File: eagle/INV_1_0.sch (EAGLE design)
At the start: 12 parts, among them IC1 74HC04N, IC2 74HC04N, X1 In A, X2 In B, X3 Out A, X4 Out B

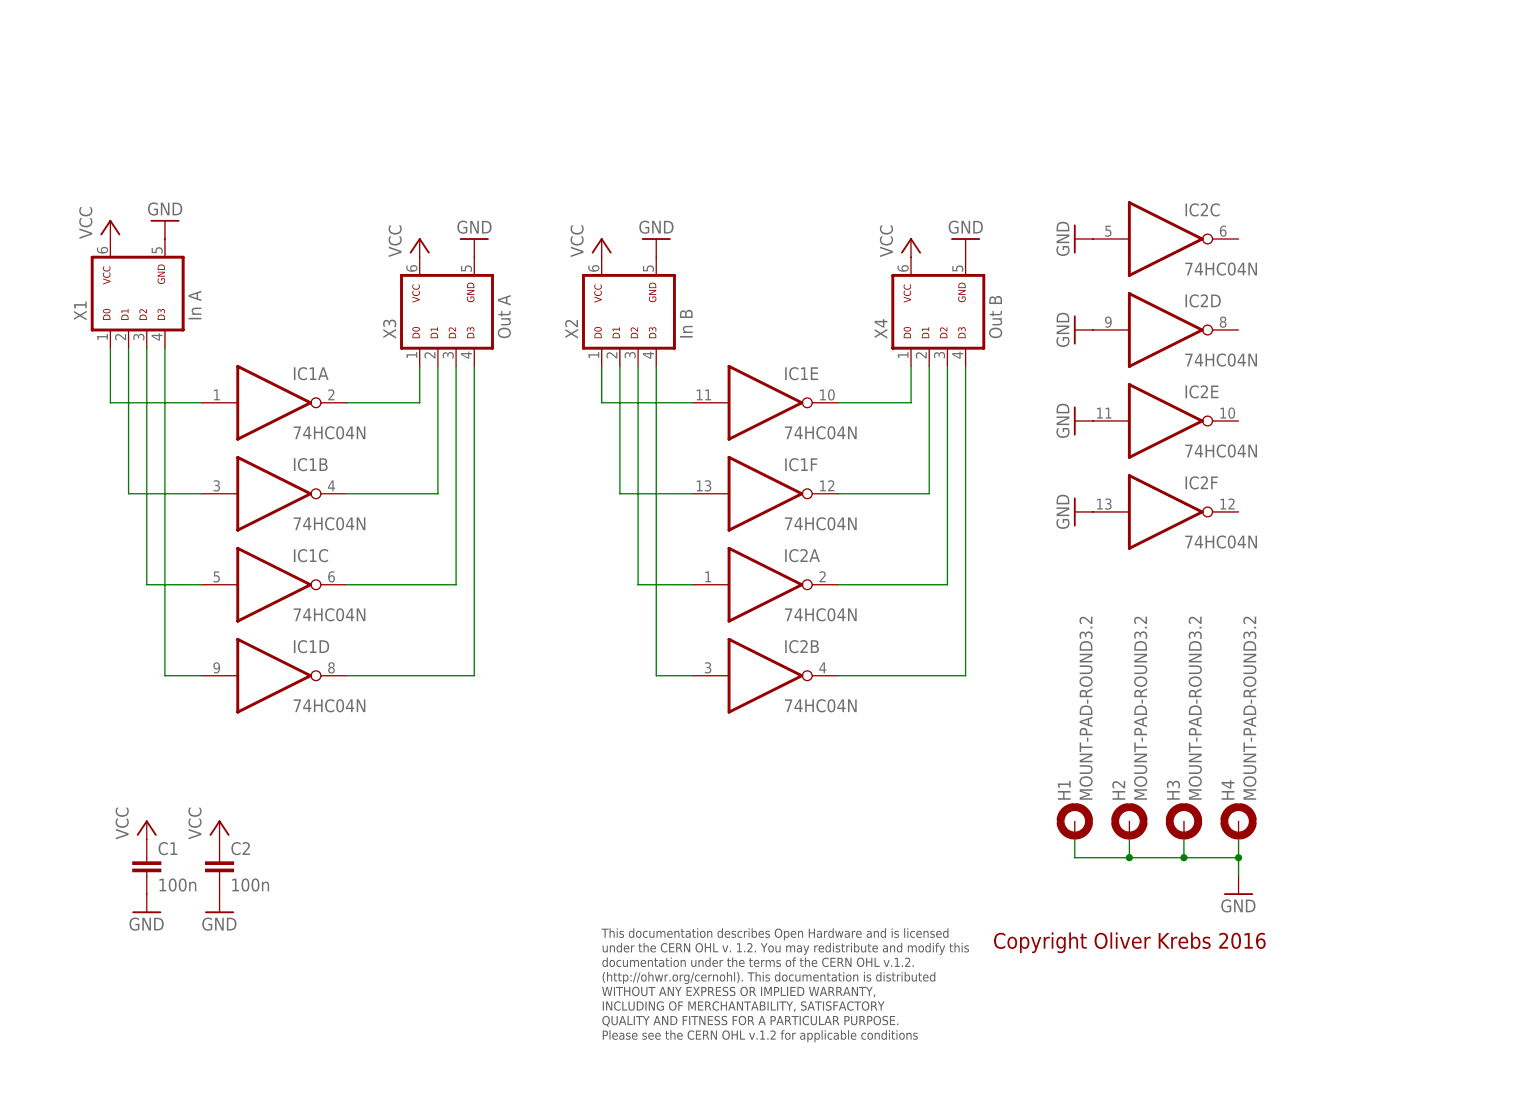
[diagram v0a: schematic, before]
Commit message: Add new tetra-Board and arduino files
Add AMP_1_0, AVC_1_0, D18_1_1, IOP_1_2, MIC_1_0, PIN_1_1, POT_1_0, PWA_1_0, PWR_1_0, RGF 2.0, SOC_2_0, VLT_1_0
Add mex_nano_shield_keyboard, mex_nano_shied_numbers

New arduino projects
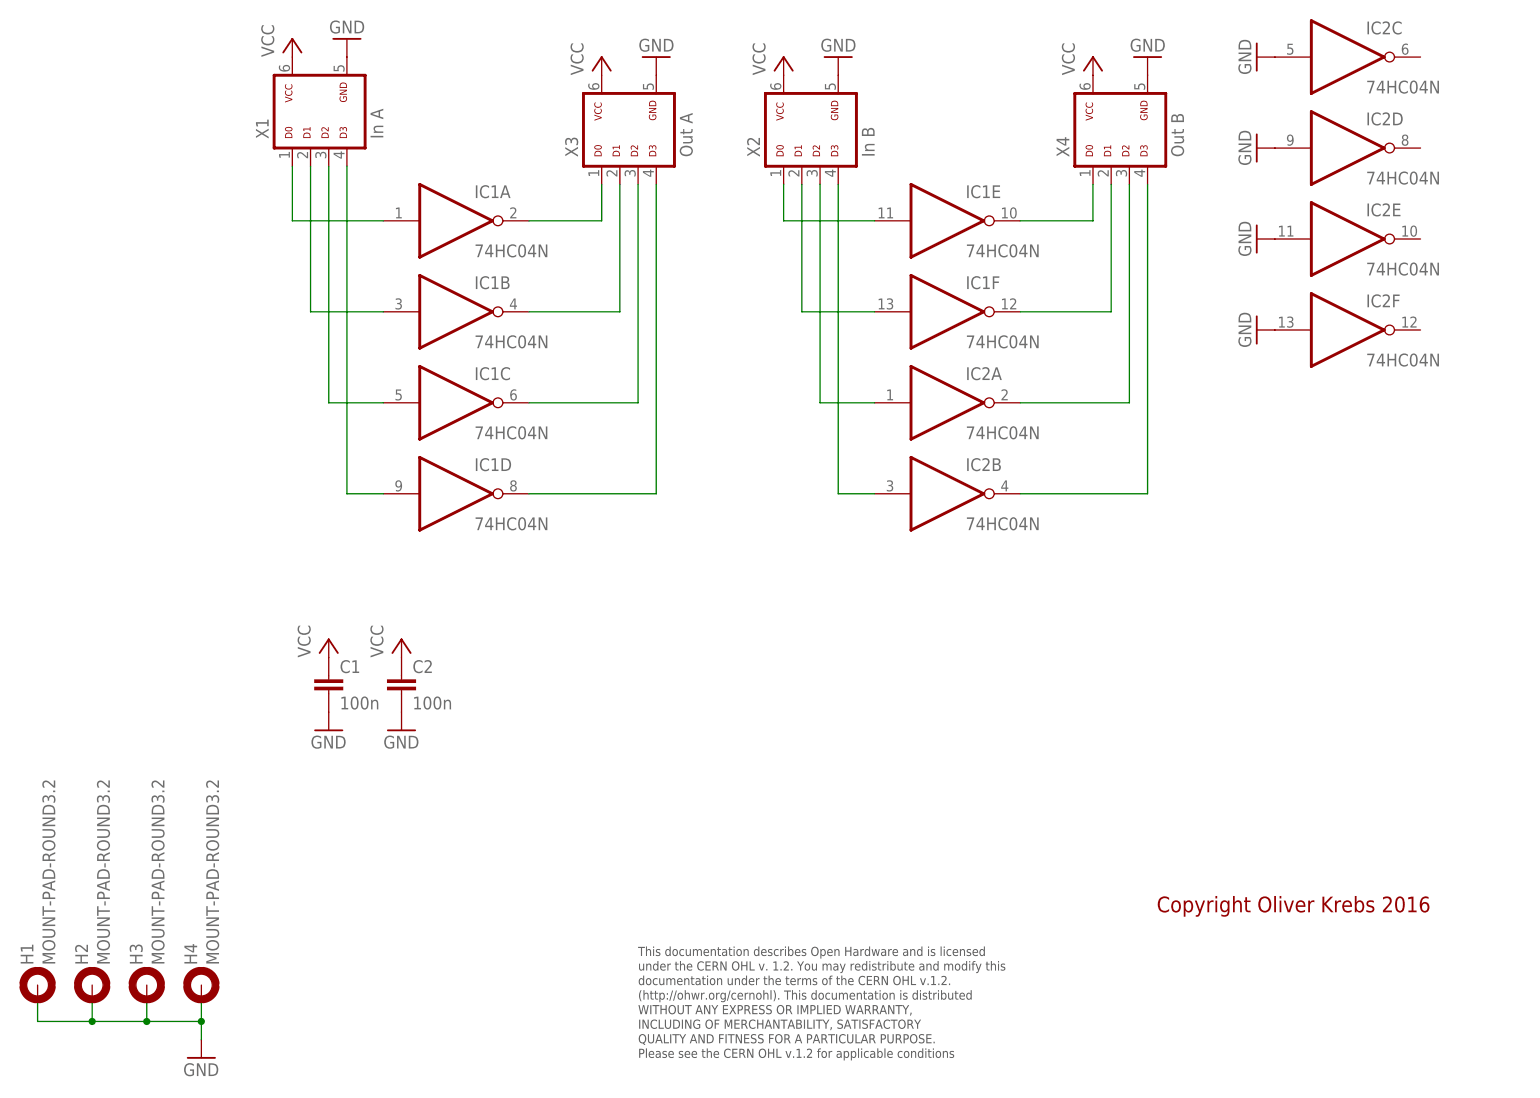
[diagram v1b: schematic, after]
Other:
- moved on the sheet: C1, C2, H1, H2, H3, H4, IC1A, IC1B, IC1C, IC1D, IC1E, IC1F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
